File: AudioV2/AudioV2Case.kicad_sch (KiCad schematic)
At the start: 0 parts

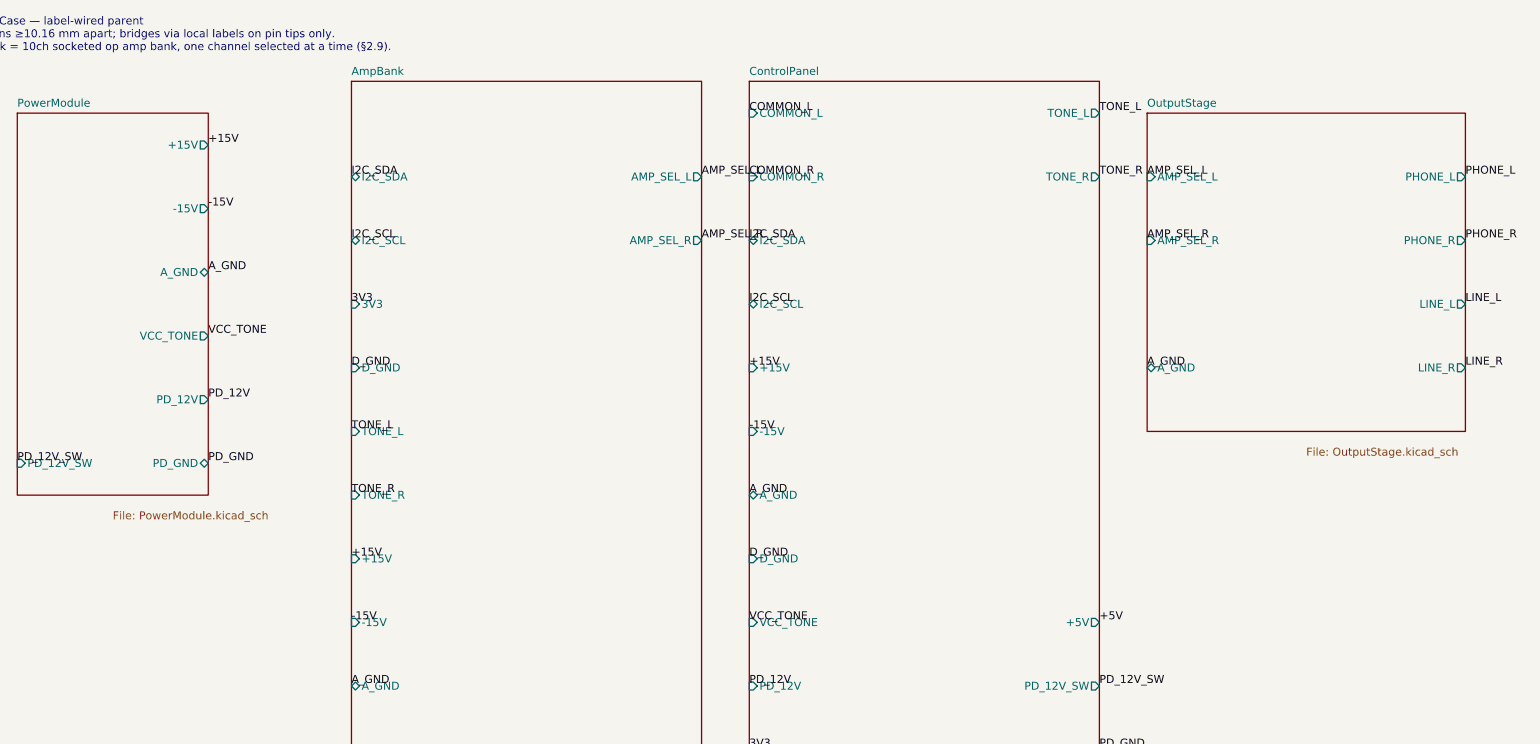
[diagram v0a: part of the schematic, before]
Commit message: AudioV2: ControlPanel の死んだインタフェース(-15V / +5V)を削除
ERC の仕分けで見つかった2件目。どちらも旧アーキテクチャの名残。

-15V: ControlPanel は +15V しか使わない（BP5293 の入力）。受け取るだけで
      中で誰も使っておらず label_dangling になっていた。
+5V : BP5293 の出力を旧 RelayBoard の AZ850 コイル用に外へ出していたが、
      アナログスイッチ化で消費先が消えた。いまは D404 経由で Pico VSYS が
      内部で使うだけなので外へ出す意味がない。

ControlPanel と親はどちらも生成コード所有なので、control_panel_wired() の
buses と parent_wired() の control_pins / join() から外して再生成した。

配電が壊れていないことをネットリストで確認:
  /+15V 48ノード（DC-DC U201.6、BP5293、LM7809、NE5532 x10 の V+、TMUX x10 の VDD）
  /-15V 46ノード（U201.4、NE5532 の V-、TMUX の VSS）。ControlPanel のノードは無し
  /ControlPanel/+5V   シート内ローカルへ降格（BP5293 VOUT -> D404 アノード）
  /ControlPanel/VSYS  D404 カソード -> Pico VSYS
親の ControlPanel シートピンは 16 -> 14 本。

ERC 55 -> 53（label_dangling 6 -> 4、残りは箱外スタブの PHONE/LINE のみ）。
check_sexpr 9/0、drift 生成コード所有 2/2 一致、BOM --check rc=0。

Co-Authored-By: Claude Opus 5 <noreply@anthropic.com>
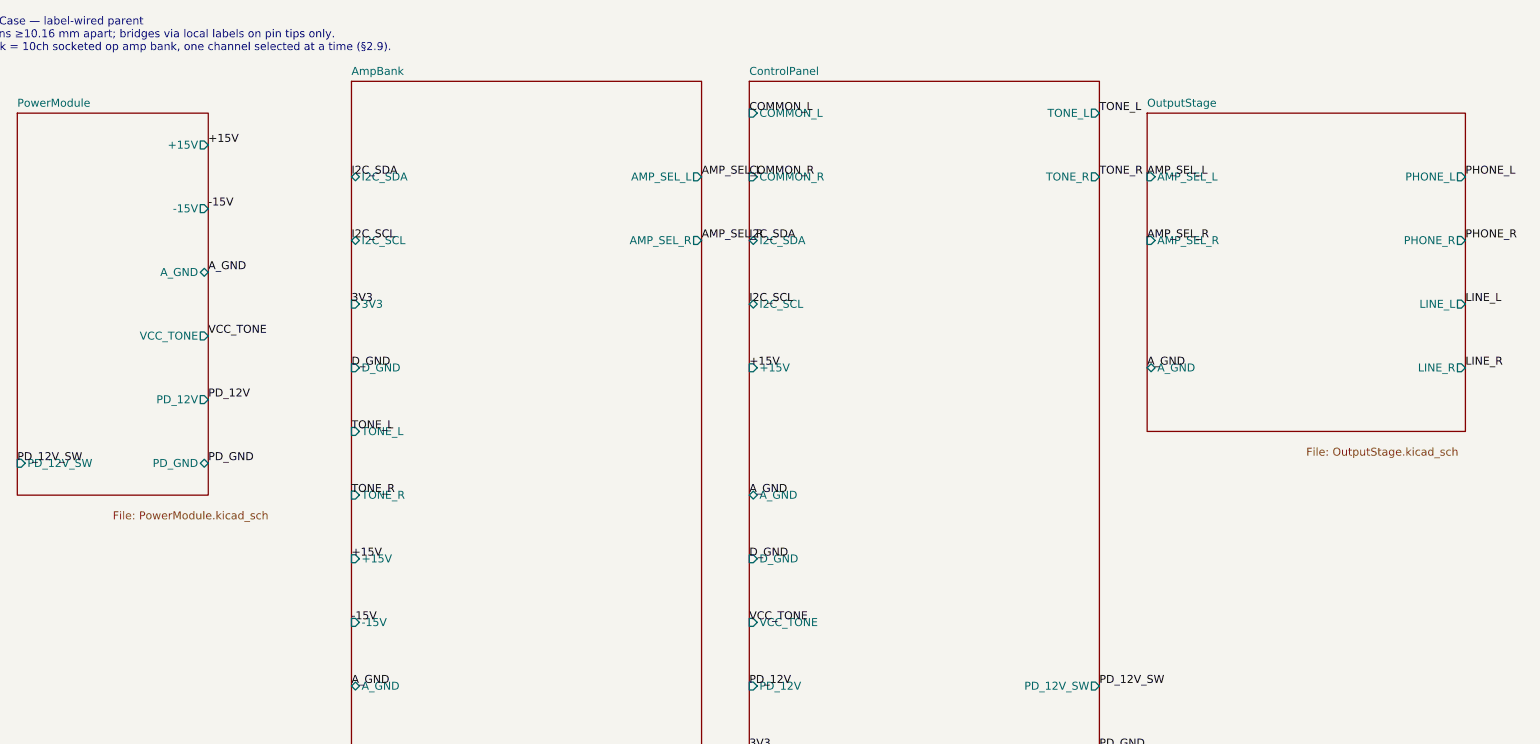
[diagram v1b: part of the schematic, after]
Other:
- sheet ControlPanel ports: added none; removed +5V, -15V

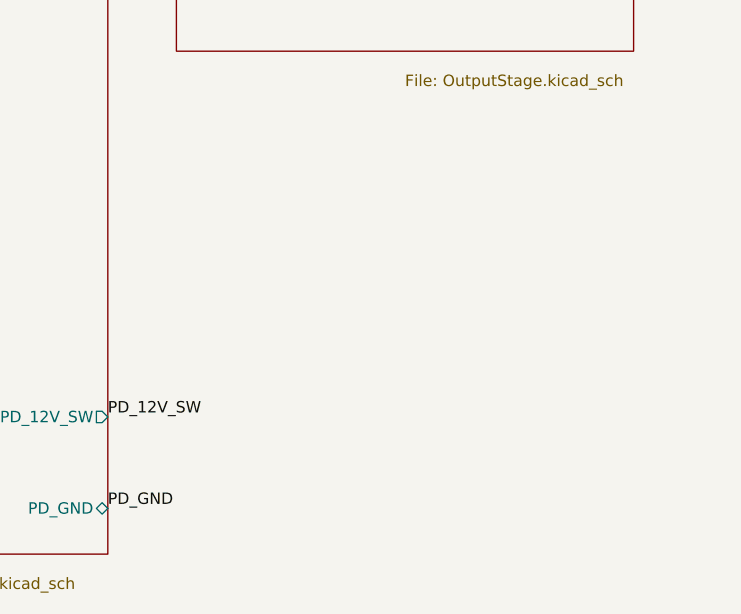
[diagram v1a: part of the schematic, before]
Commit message: AudioV2: MeasureControl シートを追加（v1 MeasurementADC からコピー）
D10（MCU 統合）で測定基板に OLED とエンコーダも載せることになったので、
回路図を AudioV2 側へ持ち込んだ。ヘッダのピン割当（スタック規格）を決めるには
基板をまたぐ信号一覧が要り、それがネットリストで機械的に出せるようになる。

■ やったこと

- Audio/MeasurementADC1804_Module.kicad_sch を AudioV2/MeasureControl.kicad_sch へコピー
  （移動ではない。Audio/ 側は実機の記録として残す。BRINGUP/STATUS もそちらを指す）
- sym-lib-table に MeasurementADC1804 / MeasurementADC_Extras を追加
  （${KIPRJMOD}/../Audio/ 参照なのでシンボルは共有。複製しない）
- AudioV2Case.kicad_sch にシートを追加（A4 の空き領域 215.9,96.52 へ配置）

■ 直した3点（どれも最初に見落としていた）

1. instances の project 名が "AudioCase" のままだった → "AudioV2Case" へ（92箇所）
2. instances の path が 1段だった → 既存シートと同じ /ルート/シート の2段へ（92箇所）
3. **参照が 7xx 帯で AmpBank/AmpCh3 と衝突していた** → 16xx 帯へ改番（180箇所）

3 が本命だった。最初の衝突チェックで各シートファイルの静的な参照しか見ておらず、
AmpChannel が10回インスタンス化されて 600〜1500番台を占めることを見落としていた。
空き帯は 100 と 1600 以降だったので 1600 番台にした。

■ 検証

  check_sexpr        10ファイル / 問題 0
  ネットリスト        注釈警告なし。部品 393 個すべてユニーク（重複 0）
  MeasureControl     84 部品が /MeasureControl/ に出る
  ERC                64件（追加前 53件、+11）

■ 境界信号（スタック規格 A2 の入力データ）

  +15V_A / -15V_A / A_GND / ADC_V_IN / ADC_GND_IN / AUDIO_L_IN / AUDIO_R_IN

Co-Authored-By: Claude Opus 5 <noreply@anthropic.com>
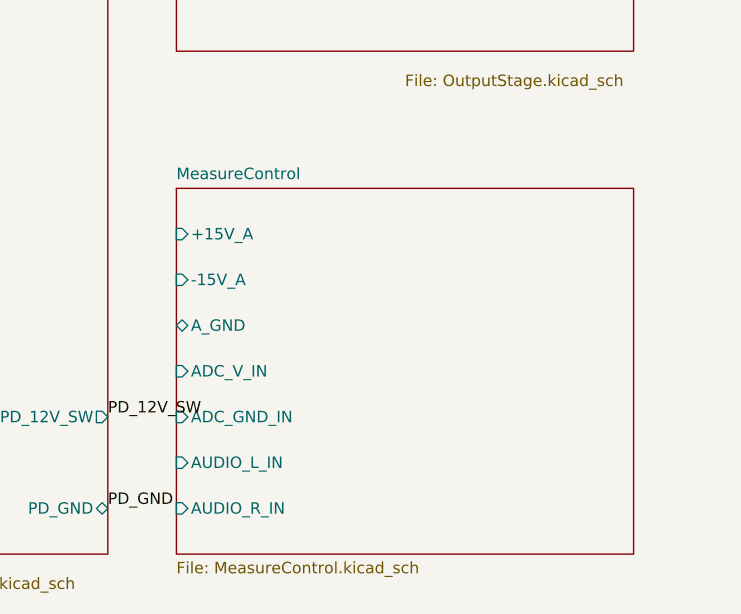
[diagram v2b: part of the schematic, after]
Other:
- added sheet MeasureControl (MeasureControl.kicad_sch)
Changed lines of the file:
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@@
+		)
+	)
+	(sheet
+		(at 215.9 96.52)
+		(size 50.8 40.64)
+		(exclude_from_sim no)
+		(in_bom yes)
+		(on_board yes)
+		(dnp no)
+		(stroke
+			(width 0.1524)
+			(type solid)
+		)
+		(fill
+			(color 0 0 0 0)
+		)
+		(property "Sheetname" "MeasureControl"
+			(at 215.9 95.6484 0)
+			(show_name no)
+			(do_not_autoplace no)
+			(effects
+				(font
+					(size 1.27 1.27)
+				)
+				(justify left bottom)
+			)
+		)
+		(property "Sheetfile" "MeasureControl.kicad_sch"
+			(at 215.9 137.96 0)
+			(show_name no)
+			(do_not_autoplace no)
+			(effects
+				(font
+					(size 1.27 1.27)
+				)
+				(justify left top)
+			)
+		)
+		(pin "+15V_A" input
+			(at 215.9 101.60 180)
+			(effects
+				(font
+					(size 1.27 1.27)
+				)
+				(justify left)
+			)
+		)
+		(pin "-15V_A" input
+			(at 215.9 106.68 180)
+			(effects
+				(font
+					(size 1.27 1.27)
+				)
+				(justify left)
+			)
+		)
+		(pin "A_GND" bidirectional
+			(at 215.9 111.76 180)
+			(effects
+				(font
+					(size 1.27 1.27)
+				)
+				(justify left)
+			)
+		)
+		(pin "ADC_V_IN" input
+			(at 215.9 116.84 180)
+			(effects
+				(font
+					(size 1.27 1.27)
+				)
+				(justify left)
+			)
+		)
+		(pin "ADC_GND_IN" input
+			(at 215.9 121.92 180)
+			(effects
+				(font
+					(size 1.27 1.27)
+				)
+				(justify left)
+			)
+		)
+		(pin "AUDIO_L_IN" input
+			(at 215.9 127.00 180)
+			(effects
+				(font
+					(size 1.27 1.27)
+				)
+				(justify left)
+			)
+		)
+		(pin "AUDIO_R_IN" input
+			(at 215.9 132.08 180)
+			(effects
+				(font
+					(size 1.27 1.27)
+				)
+				(justify left)
+			)
 		)
 	)

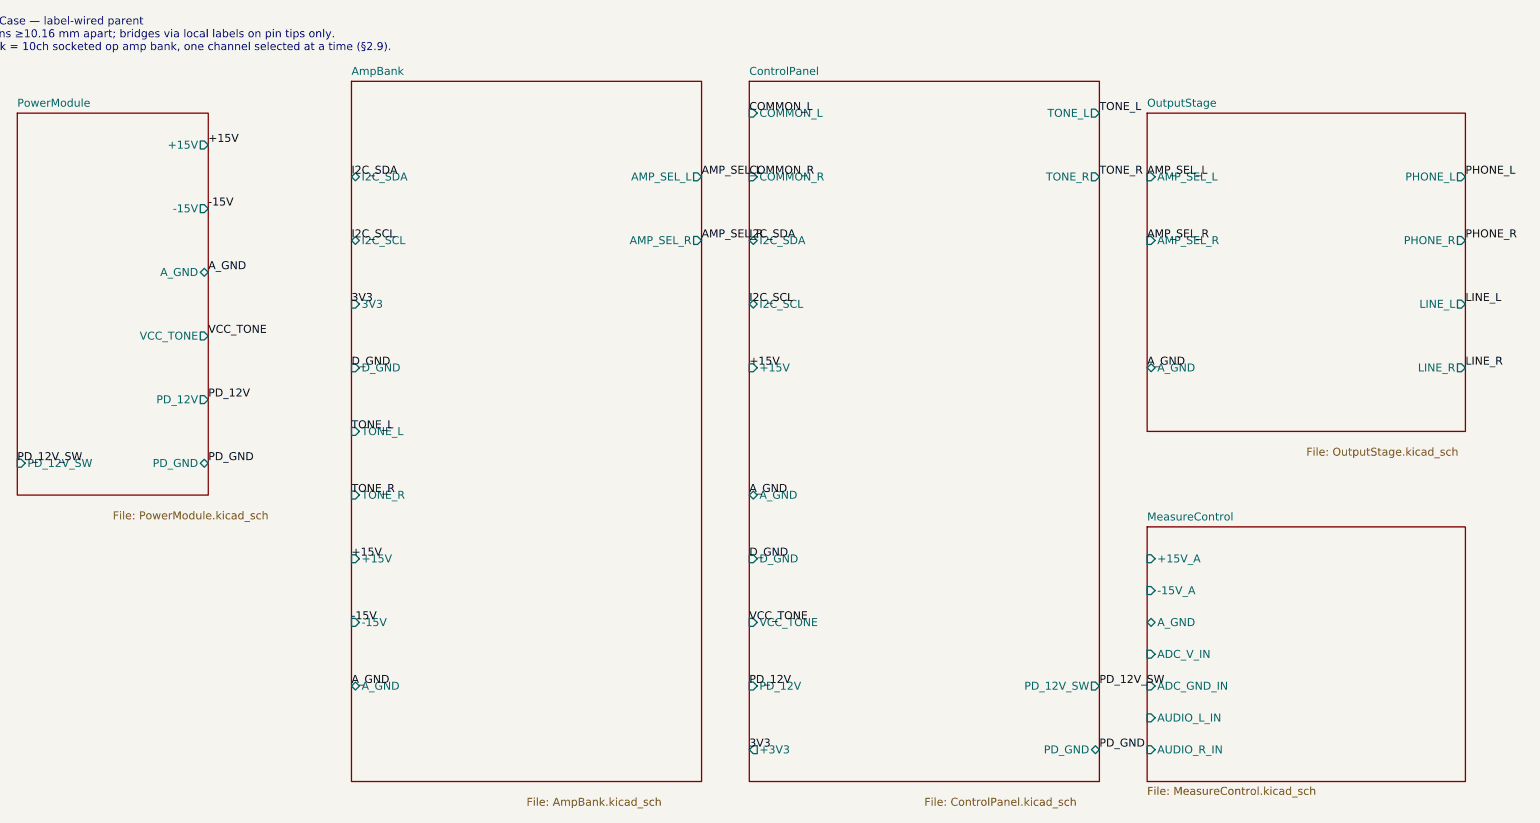
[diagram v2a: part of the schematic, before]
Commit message: AudioV2: MeasureControl を親に結線（KiCad 手編集）
親で MeasureControl シートを (238.76, 91.44) に配置し、7本のシートピンを
ラベル＋短いワイヤで親のネットに接続した。ネットリストで合流を確認:

  +15V_A      -> /+15V       (U1601/U1602/U1608 の V+、パスコン5個)
  -15V_A      -> /-15V       (同 V-、パスコン5個)
  A_GND       -> /A_GND      (NT1601 経由でアナロググランドへ)
  ADC_V_IN    -> /PD_12V_SW  (F1601 -> U1604/U1607)
  ADC_GND_IN  -> /PD_GND     (NT1602 経由)
  AUDIO_L_IN  -> /AMP_SEL_L  (選択された Amp の出力)
  AUDIO_R_IN  -> /AMP_SEL_R

GND は v1 の NetTie 構造がそのまま効いており、ADC_GND と D_GND が
それぞれ1点だけで親の A_GND / PD_GND に落ちる。

ADC_V_IN に PWR_FLAG を追加（駆動側が SW402/D403 の passive しか無く
U1604 IN+ が power_pin_not_driven になっていた）。

ControlPanel: -15V(input) / +5V(output) の階層ピンを追加し、
+5V -> ショットキー -> VSYS のローカル給電（D404 / PWR_FLAG）を削除。
※ この結果 U401(Pico) の VSYS ピンが浮いている。Pico を
  ControlPanel と MeasureControl のどちらに寄せるかは未決定。

ERC 64 -> 60。MeasureControl の違反は 4件 -> 0件。
部品 392 個すべてユニーク（重複 0、注釈警告なし）。

Co-Authored-By: Claude Opus 5 <noreply@anthropic.com>
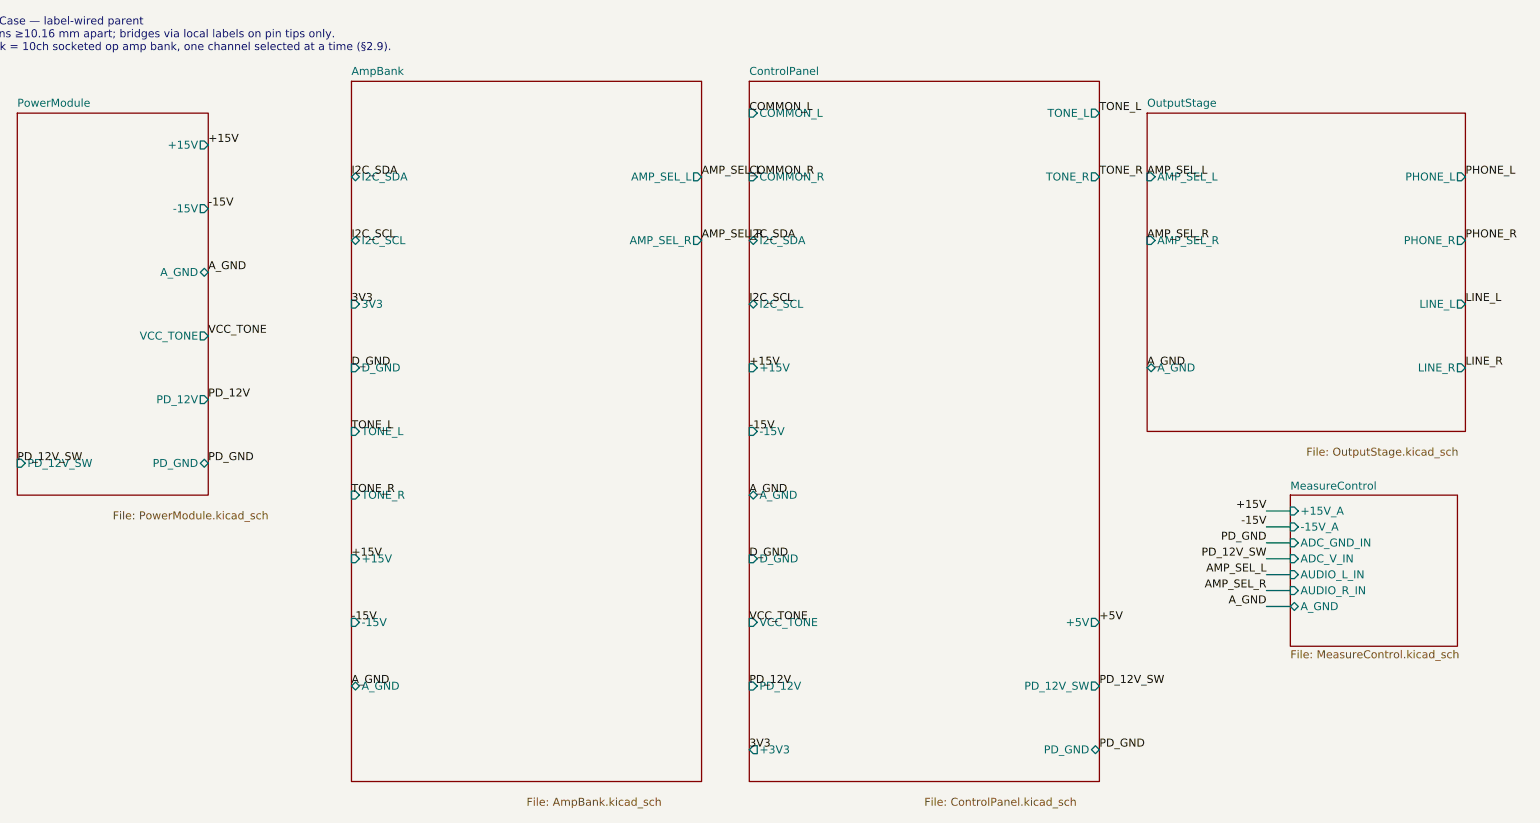
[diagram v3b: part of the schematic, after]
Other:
- sheet ControlPanel ports: added +5V, -15V; removed none
